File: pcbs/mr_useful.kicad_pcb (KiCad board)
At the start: 2 copper layers, 57 x 95 mm, 37 parts

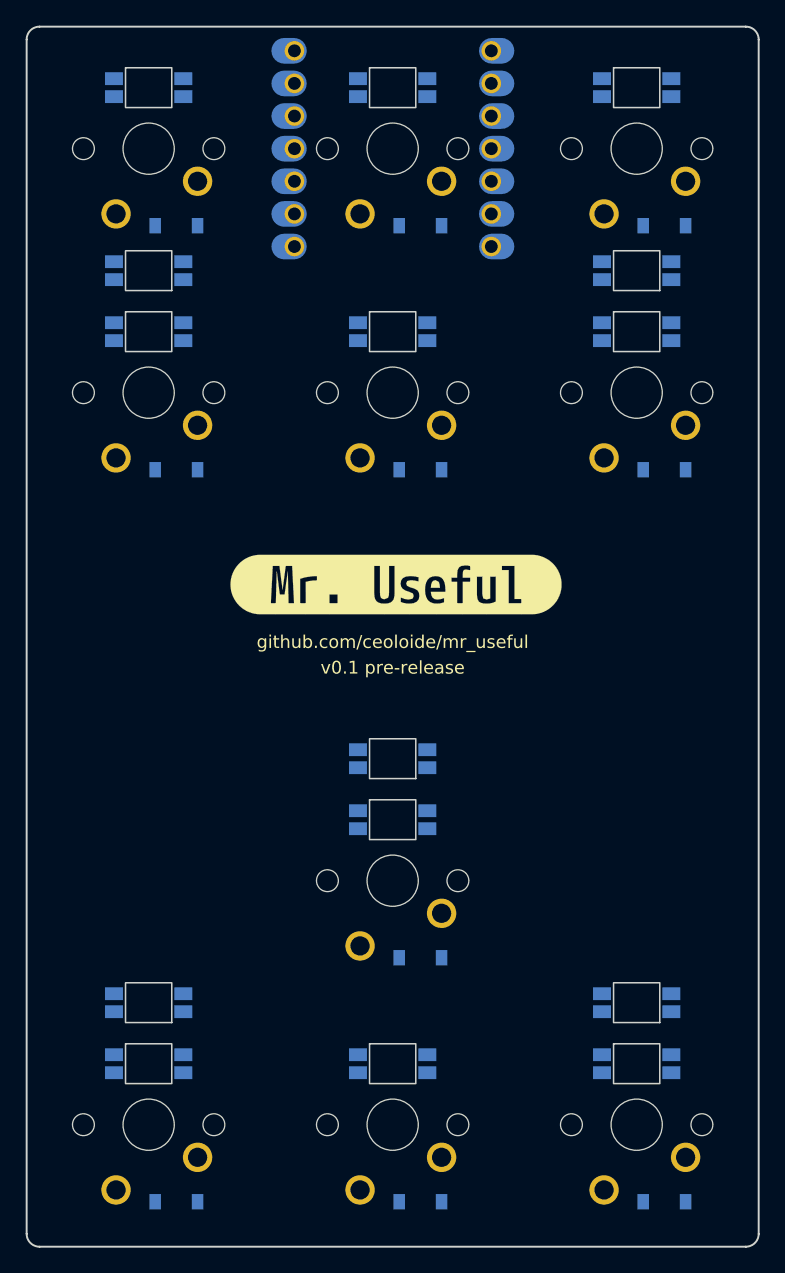
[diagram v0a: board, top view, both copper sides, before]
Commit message: Update MX switch footprint
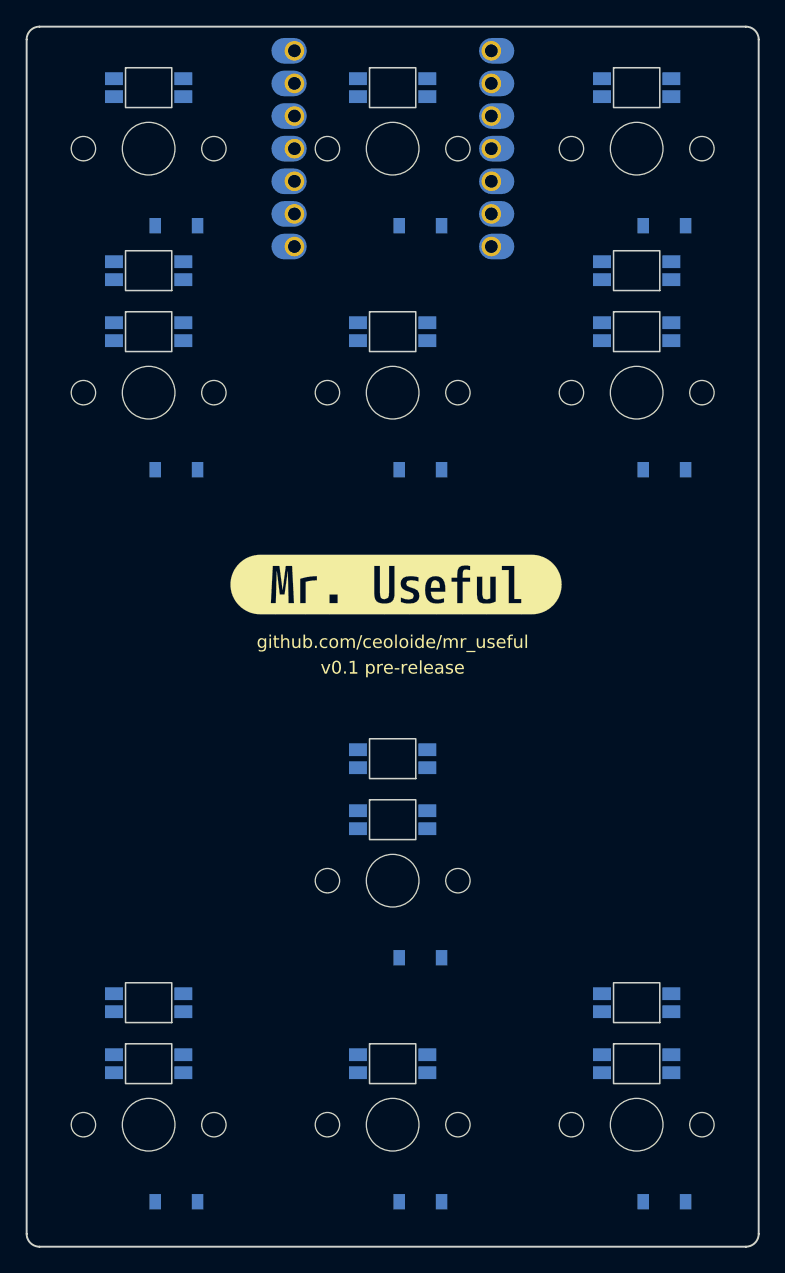
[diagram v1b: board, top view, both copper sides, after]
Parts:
- S1, S10, S2, S3, S4, S5, S6, S7, S8, S9: footprint MX -> ceoloide:switch_mx; moved to B.Cu
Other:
- net class Default removed
